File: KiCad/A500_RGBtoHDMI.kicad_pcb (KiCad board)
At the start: 2 copper layers, 80 x 29.5 mm, 5 parts, among them J1 Conn_02x20_Odd_Even, U1 Denise_Socket, U2 XC9572XL-VQ64, U3 Denise_MB_PinHeader

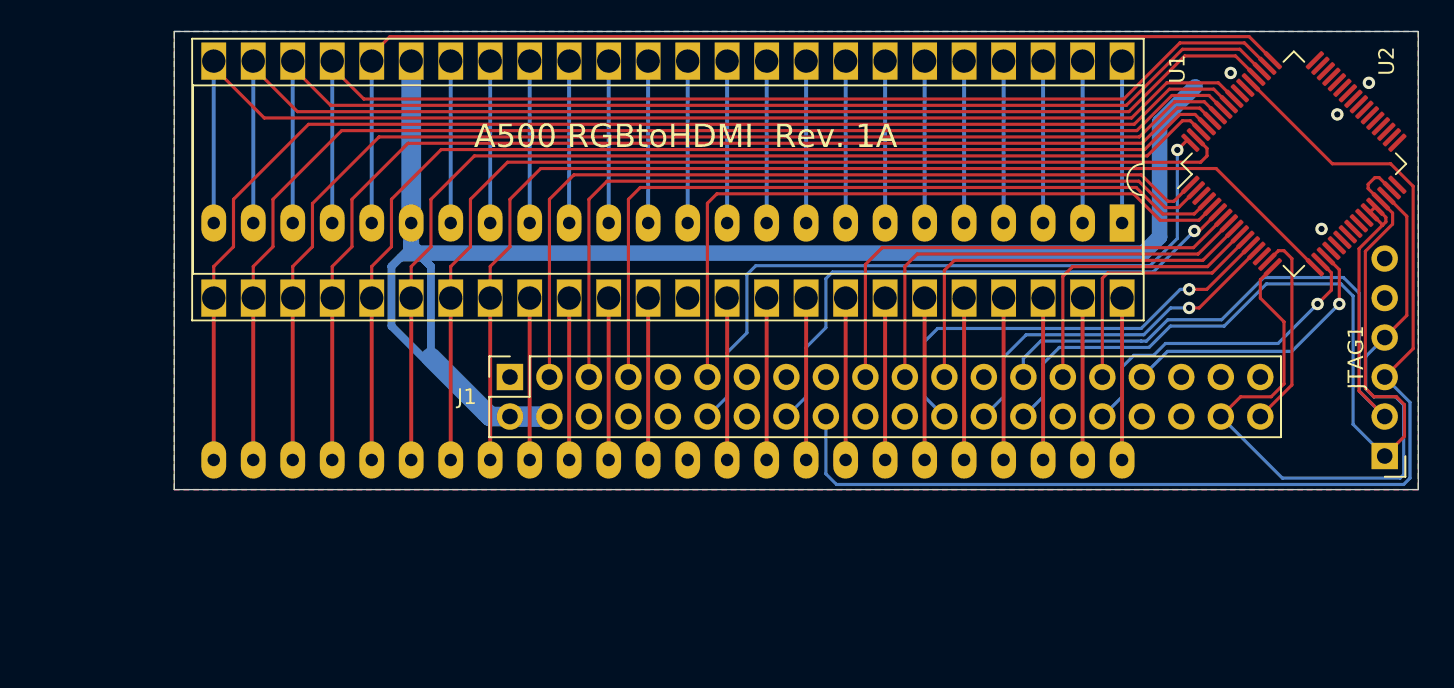
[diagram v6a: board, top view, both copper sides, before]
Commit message: added LDO LM1117 3.3V fixed output
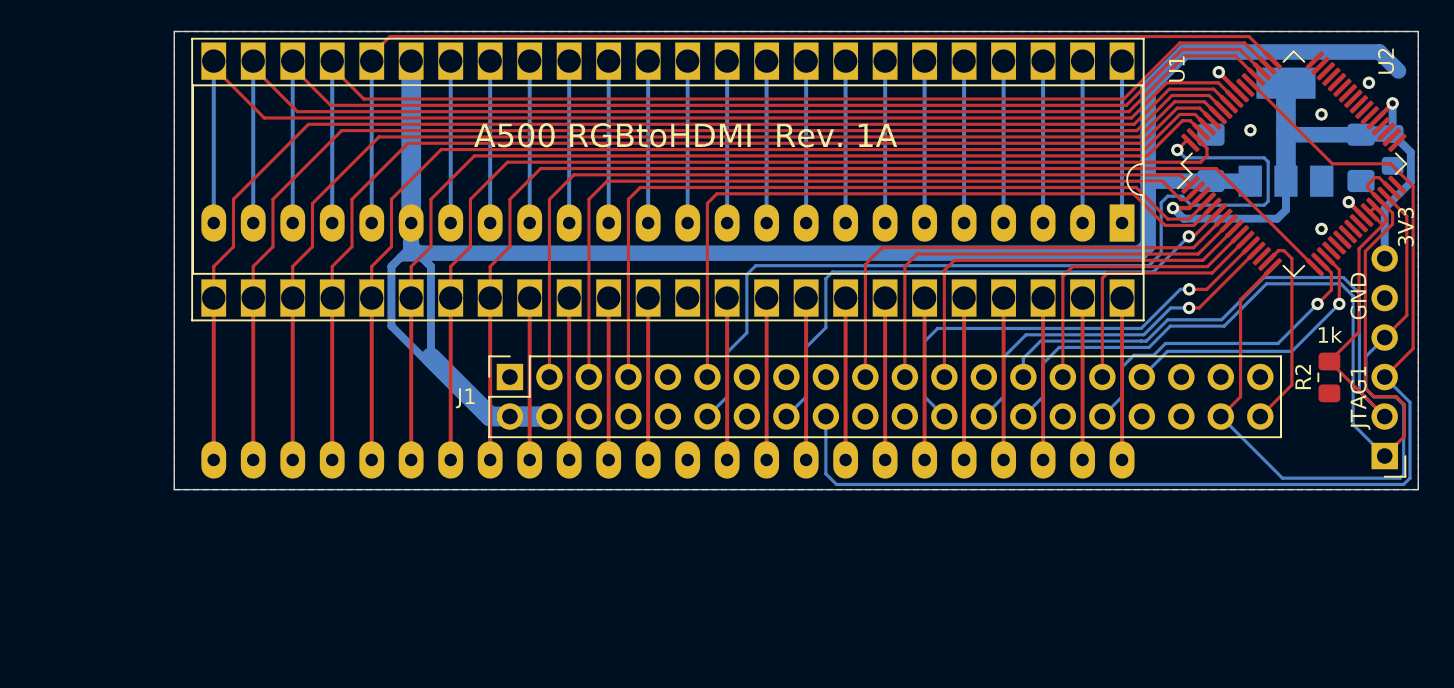
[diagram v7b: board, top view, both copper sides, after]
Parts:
- added C1: 10uF, Capacitor_SMD:C_1206_3216Metric_Pad1.42x1.75mm_HandSolder, B.Cu at (193.7, 83.9)
- added C2: 10uF, Capacitor_SMD:C_1206_3216Metric_Pad1.42x1.75mm_HandSolder, B.Cu at (203.3, 83.9)
- added C3: 0.1uF, Capacitor_SMD:C_0805_2012Metric_Pad1.15x1.40mm_HandSolder, B.Cu at (205.4, 83.4)
- added R2: 1k, Resistor_SMD:R_0805_2012Metric_Pad1.15x1.40mm_HandSolder, F.Cu at (201.3, 98.1)
- added U3: LM1117-3.3, Package_TO_SOT_SMD:SOT-223, B.Cu at (198.5, 82.3)
- renumbered U3 to U4
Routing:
- net 3V3: track 0.00 -> 41.1 mm, vias 0 -> 4
- net VCC: track 115.4 -> 138.1 mm
- net VERSION: track 45.7 -> 57.9 mm
- net TCK_SPCLK: track 48.3 -> 45.9 mm
- net TDI_SPDATA: track 50.8 -> 52.4 mm
- net B0_3V3: track 54.4 -> 53.6 mm
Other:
- board text added: "1k"
- board text added: "3V3"
- board text added: "GND"

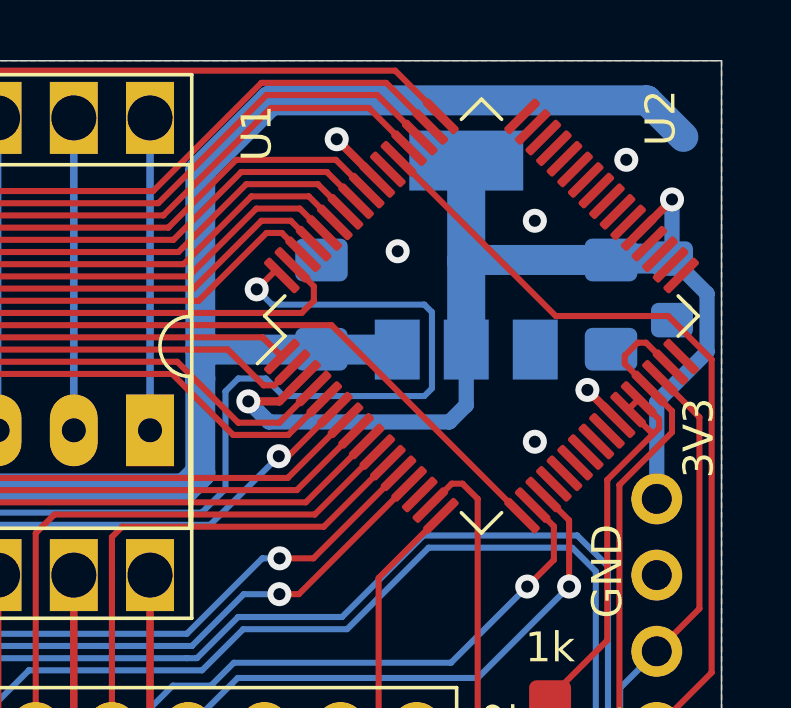
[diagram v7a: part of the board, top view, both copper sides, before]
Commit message: added 100nF decoupling caps to CPLDs 3V3-inputs
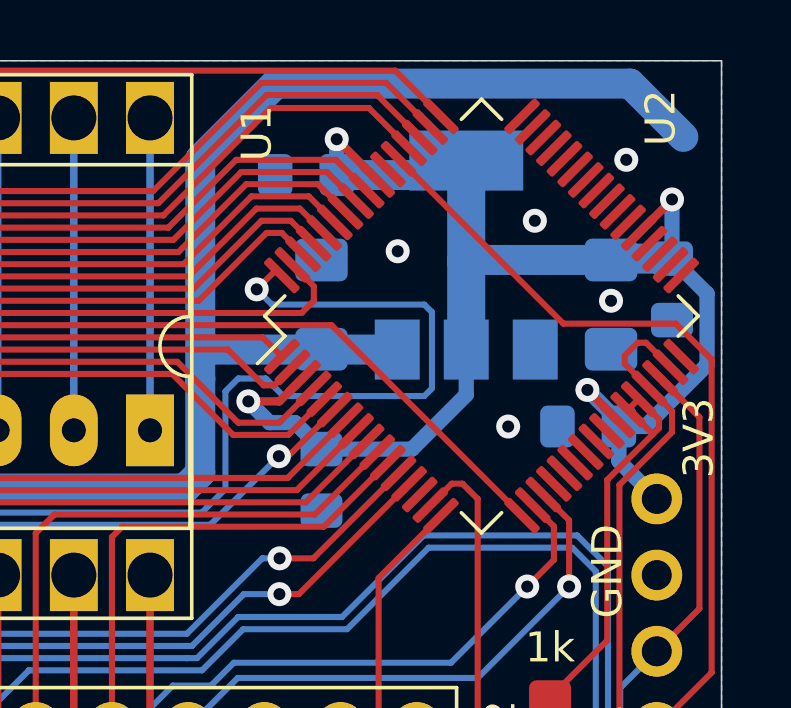
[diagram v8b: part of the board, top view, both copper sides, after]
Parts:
- added C4: 0.1uF, Capacitor_SMD:C_0805_2012Metric_Pad1.15x1.40mm_HandSolder, B.Cu at (193.2, 79.6)
- added C5: 0.1uF, Capacitor_SMD:C_0805_2012Metric_Pad1.15x1.40mm_HandSolder, B.Cu at (202.6, 88.0)
- added C6: 0.1uF, Capacitor_SMD:C_0805_2012Metric_Pad1.15x1.40mm_HandSolder, B.Cu at (193.7, 89.8)
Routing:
- net 3V3: track 41.1 -> 50.5 mm
- net VCC: track 138.1 -> 138.8 mm
- net GND: vias 4 -> 5
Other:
- board text added: "TCK"
- board text added: "TDI"
- board text added: "TDO"
- board text added: "TMS"
